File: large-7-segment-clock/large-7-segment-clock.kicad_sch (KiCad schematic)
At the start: 25 parts, among them J1 USB_B_Micro, U1 MCP2221AxP, U2 4-digit-clock, U3 ESP-01S, U4 TM1637, U5 LM317_TO-220

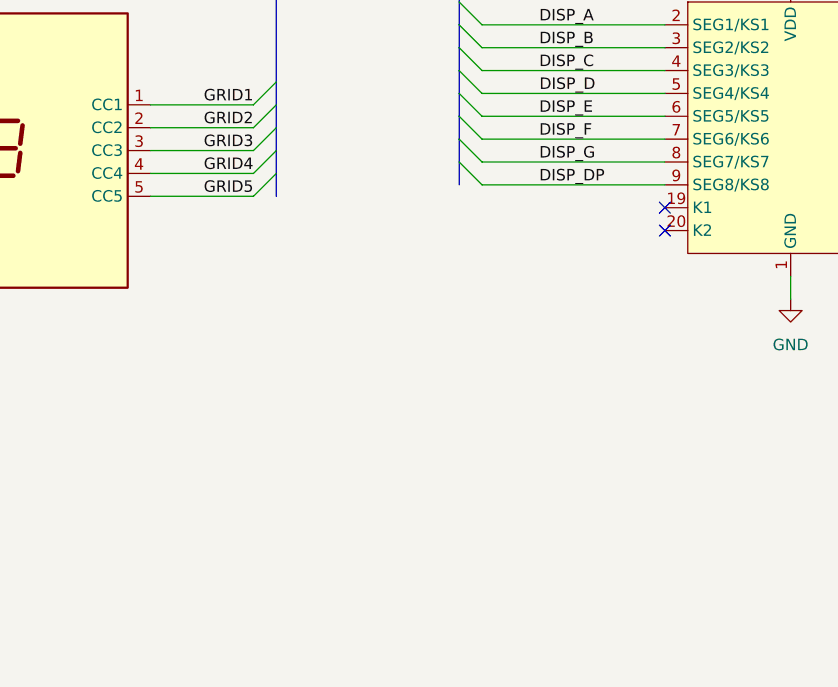
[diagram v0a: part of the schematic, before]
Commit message: Added switches for user interface
Signed-off-by: Matthew Nickson <mnickson@sidingsmedia.com>
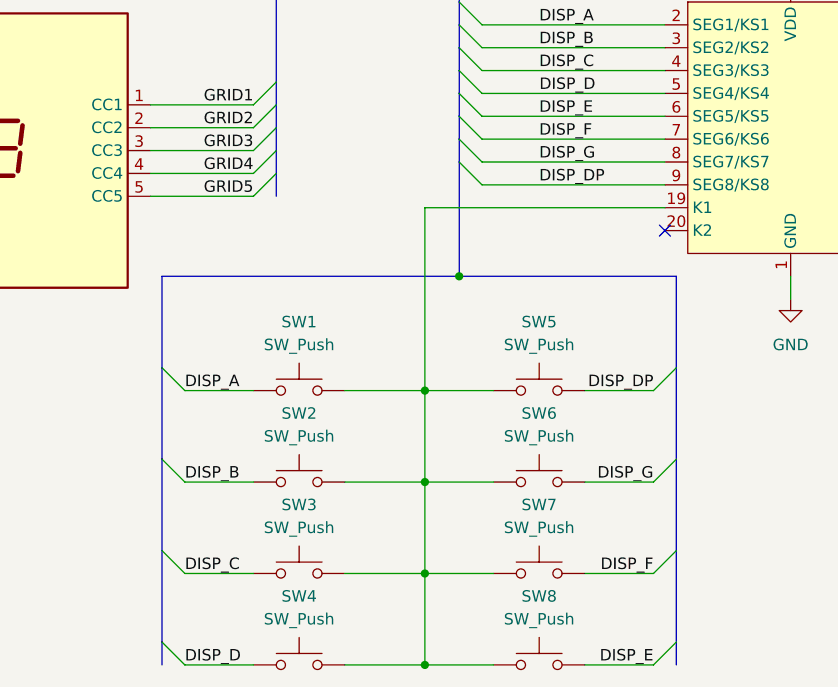
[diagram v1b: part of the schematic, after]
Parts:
- added SW1, SW2, SW3, SW4, SW5, SW6, SW7, SW8: SW_Push, symbol Switch:SW_Push
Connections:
- net DISP_A: now also SW1.1
- net DISP_B: now also SW2.1
- net DISP_C: now also SW3.1
- net DISP_D: now also SW4.1
- net DISP_DP: now also SW5.2
- net DISP_E: now also SW8.2
- net DISP_F: now also SW7.2
- net DISP_G: now also SW6.2
- net at U4.19 (K1): now also SW1.2, SW2.2, SW3.2, SW4.2, SW5.1, SW6.1, SW7.1, SW8.1
- no-connect marks 7 -> 6
